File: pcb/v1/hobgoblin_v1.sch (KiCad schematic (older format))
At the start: 28 parts

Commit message: Finish the schematic
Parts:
- removed R?: 10K, symbol Device:R
- removed SW?: ROMBNK, symbol Switch:SW_DIP_x01
- removed U?: 74LS32, symbol 74xx:74LS32
- removed U?: 28C256, symbol Memory_EEPROM:28C256
- added C10, C11, C12, C2, C3, C4, C5, C6, C7, C8, C9: 0.1uF, Capacitor_THT:C_Disc_D3.8mm_W2.6mm_P2.50mm, symbol Device:C
- added CF1: CF_Socket, Connector_Card:CF-Card_3M_N7E50-7516PK-20-WF, symbol hobgoblin:CF_Socket
- added D2: CF, LED_THT:LED_D5.0mm, symbol Device:LED
- added D5: ON, LED_THT:LED_D5.0mm, symbol Device:LED
- added J1: 5V, Connector_BarrelJack:BarrelJack_Horizontal, symbol Connector:Barrel_Jack
- added J2: RC2014EXT1, Connector_PinHeader_2.54mm:PinHeader_1x40_P2.54mm_Vertical, symbol Connector_Generic:Conn_01x40
- added J3: RC2014EXT2, Connector_PinHeader_2.54mm:PinHeader_1x40_P2.54mm_Vertical, symbol Connector_Generic:Conn_01x40
- added R10, R14, R7, R8, R9: 1K, Resistor_THT:R_Axial_DIN0207_L6.3mm_D2.5mm_P10.16mm_Horizontal, symbol Device:R
- added R11: 330, Resistor_THT:R_Axial_DIN0207_L6.3mm_D2.5mm_P10.16mm_Horizontal, symbol Device:R
- added R4, R5, R6: 10K, Resistor_THT:R_Axial_DIN0207_L6.3mm_D2.5mm_P10.16mm_Horizontal, symbol Device:R
- added SW2: ROMBNK, Button_Switch_THT:SW_DIP_SPSTx03_Slide_6.7x9.18mm_W7.62mm_P2.54mm_LowProfile, symbol Switch:SW_DIP_x03
- added unit 3 of U7
- added unit 5 of U7
- added U8: SST39SF010, Package_DIP:DIP-32_W15.24mm_LongPads, symbol Memory_Flash:SST39SF010
- C1: renamed from C?; footprint (none) -> Capacitor_THT:C_Disc_D3.8mm_W2.6mm_P2.50mm
- R1, R2, R3: renamed from R?; footprint (none) -> Resistor_THT:R_Axial_DIN0207_L6.3mm_D2.5mm_P10.16mm_Horizontal
- SW1: renamed from SW?; footprint (none) -> Button_Switch_THT:SW_PUSH_6mm
- U1, U3, U6, U7: renamed from U?; footprint (none) -> Package_DIP:DIP-14_W7.62mm_LongPads
- U2: renamed from U?; footprint (none) -> Package_DIP:DIP-40_W15.24mm_LongPads
- U4: renamed from U?; footprint (none) -> Package_DIP:DIP-16_W7.62mm_LongPads
- U5: renamed from U?; footprint (none) -> Package_DIP:DIP-32_W15.24mm_LongPads
- U9: renamed from U?; footprint Package_DIP:DIP-40_W15.24mm -> Package_DIP:DIP-24_W15.24mm_LongPads
- gave numbers to parts that had none: 3
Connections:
- net labels added: IORQ, ROMBNK0, ROMBNK1, ROMBNK2, RXD, TXD, USR1, USR2, USR3, USR4, ~RTS
- net labels removed: ROMBNK, ~IORD, ~PORT0
- wire segments 53 -> 109
- no-connect marks 10 -> 27
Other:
- moved on the sheet: U1A, U1C, U1D, U4, U5, U6A, U6C, U6D, U7A, U7B, U9, X1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

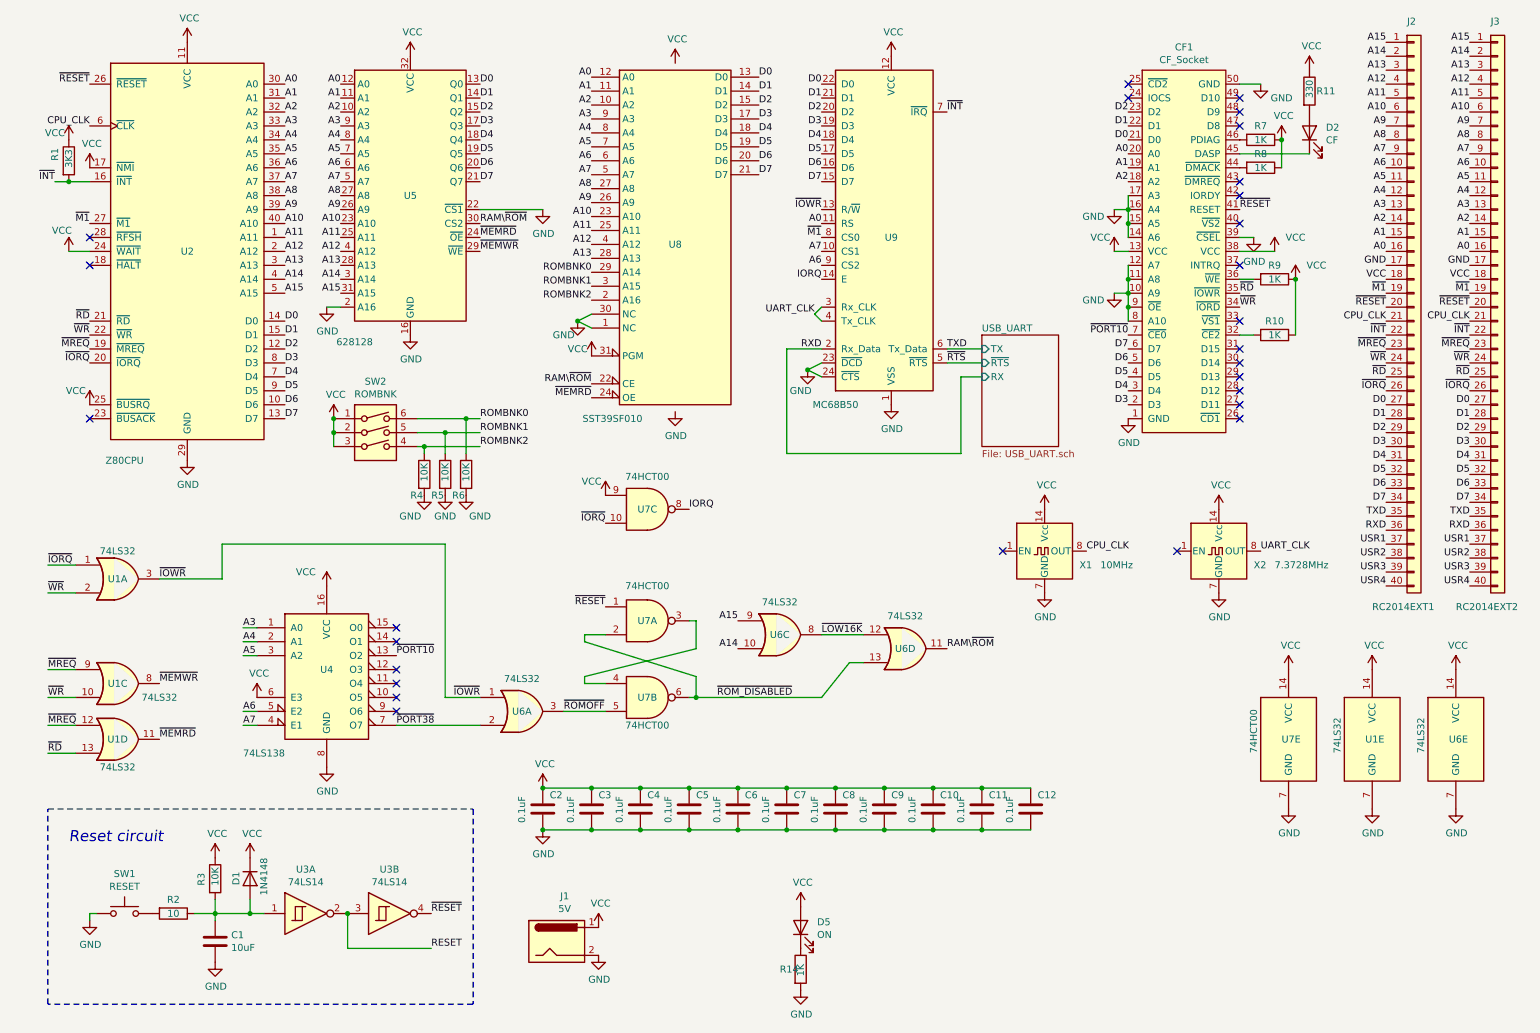
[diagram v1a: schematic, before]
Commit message: Place components on the PCB layout
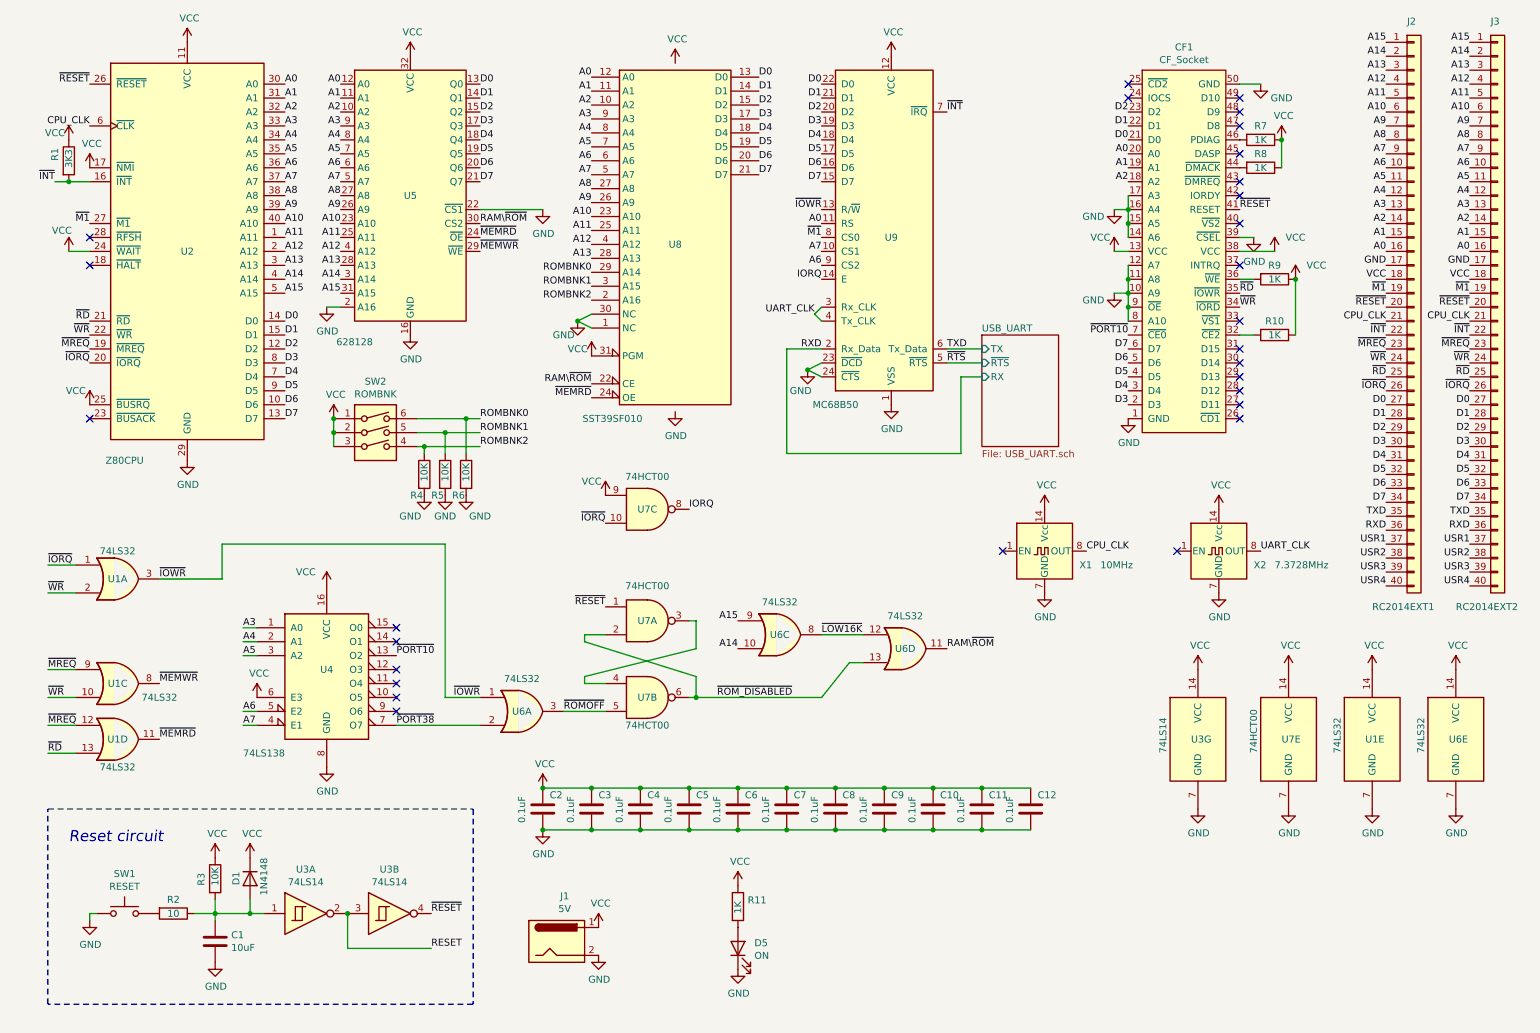
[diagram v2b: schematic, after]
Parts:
- removed D2: CF, LED_THT:LED_D5.0mm, symbol Device:LED
- removed R14: 1K, Resistor_THT:R_Axial_DIN0207_L6.3mm_D2.5mm_P10.16mm_Horizontal, symbol Device:R
- added unit 7 of U3
- J2, J3: footprint Connector_PinHeader_2.54mm:PinHeader_1x40_P2.54mm_Vertical -> hobgoblin:RC2014_Connector
- R11: value 330 -> 1K
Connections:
- net GND: now also D5.1 (K), U3.7 (GND)
- net VCC: now also U3.14 (VCC); no longer D5.2 (A)
- net at R11.2: now also D5.2 (A)
- no-connect marks 27 -> 28
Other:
- moved on the sheet: D5
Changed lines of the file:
@@
 F 0 "J3" H 10950 4650 50  0000 L CNN
 F 1 "RC2014EXT2" H 10700 450 50  0000 L CNN
-F 2 "Connector_PinHeader_2.54mm:PinHeader_1x40_P2.54mm_Vertical" H 11000 2600 50  0001 C CNN
+F 2 "hobgoblin:RC2014_Connector" H 11000 2600 50  0001 C CNN
 F 3 "~" H 11000 2600 50  0001 C CNN
 	1    11000 2600
@@
 F 0 "J2" H 10350 4650 50  0000 L CNN
 F 1 "RC2014EXT1" H 10100 450 50  0000 L CNN
-F 2 "Connector_PinHeader_2.54mm:PinHeader_1x40_P2.54mm_Vertical" H 10400 2600 50  0001 C CNN
+F 2 "hobgoblin:RC2014_Connector" H 10400 2600 50  0001 C CNN
 F 3 "~" H 10400 2600 50  0001 C CNN
 	1    10400 2600
@@
 Connection ~ 9450 1400
 $Comp
-L Device:LED D2
-U 1 1 5FF291EF
-P 9650 1350
-F 0 "D2" V 9689 1232 50  0000 R CNN
-F 1 "CF" V 9598 1232 50  0000 R CNN
-F 2 "LED_THT:LED_D5.0mm" H 9650 1350 50  0001 C CNN
-F 3 "~" H 9650 1350 50  0001 C CNN
-	1    9650 1350
-	0    -1   -1   0
-$EndComp
-Wire Wire Line
-	9650 1500 9150 1500
-$Comp
-L Device:R R11
-U 1 1 5FF2D25B
-P 9650 1050
-F 0 "R11" H 9700 1050 50  0000 L CNN
-F 1 "330" V 9650 1000 50  0000 L CNN
-F 2 "Resistor_THT:R_Axial_DIN0207_L6.3mm_D2.5mm_P10.16mm_Horizontal" V 9580 1050 50  0001 C CNN
-F 3 "~" H 9650 1050 50  0001 C CNN
-	1    9650 1050
-	1    0    0    -1
-$EndComp
-$Comp
-L power:VCC #PWR049
-U 1 1 5FF2F6DF
-P 9650 900
-F 0 "#PWR049" H 9650 750 50  0001 C CNN
-F 1 "VCC" H 9665 1073 50  0000 C CNN
-F 2 "" H 9650 900 50  0001 C CNN
-F 3 "" H 9650 900 50  0001 C CNN
-	1    9650 900
-	1    0    0    -1
-$EndComp
-$Comp
 L power:GND #PWR042
 U 1 1 5FF38D98
@@
 L Device:LED D5
 U 1 1 5FA5AC1B
-P 6000 7050
-F 0 "D5" V 6039 6932 50  0000 R CNN
-F 1 "ON" V 5948 6932 50  0000 R CNN
-F 2 "LED_THT:LED_D5.0mm" H 6000 7050 50  0001 C CNN
-F 3 "~" H 6000 7050 50  0001 C CNN
-	1    6000 7050
+P 5550 7200
+F 0 "D5" V 5589 7082 50  0000 R CNN
+F 1 "ON" V 5498 7082 50  0000 R CNN
+F 2 "LED_THT:LED_D5.0mm" H 5550 7200 50  0001 C CNN
+F 3 "~" H 5550 7200 50  0001 C CNN
+	1    5550 7200
 	0    -1   -1   0
 $EndComp
@@
 L power:GND #PWR0101
 U 1 1 5FA5C10E
-P 6000 7500
-F 0 "#PWR0101" H 6000 7250 50  0001 C CNN
-F 1 "GND" H 6005 7327 50  0000 C CNN
-F 2 "" H 6000 7500 50  0001 C CNN
-F 3 "" H 6000 7500 50  0001 C CNN
-	1    6000 7500
+P 5550 7350
+F 0 "#PWR0101" H 5550 7100 50  0001 C CNN
+F 1 "GND" H 5555 7177 50  0000 C CNN
+F 2 "" H 5550 7350 50  0001 C CNN
+F 3 "" H 5550 7350 50  0001 C CNN
+	1    5550 7350
+	1    0    0    -1
+$EndComp
+$Comp
+L 74xx:74LS14 U3
+U 7 1 6002B138
+P 8850 5700
+F 0 "U3" H 8800 5700 50  0000 L CNN
+F 1 "74LS14" V 8600 5600 50  0000 L CNN
+F 2 "Package_DIP:DIP-14_W7.62mm_LongPads" H 8850 5700 50  0001 C CNN
+F 3 "http://www.ti.com/lit/gpn/sn74LS14" H 8850 5700 50  0001 C CNN
+	7    8850 5700
+	1    0    0    -1
+$EndComp
+$Comp
+L power:VCC #PWR0104
+U 1 1 6002EF38
+P 8850 5200
+F 0 "#PWR0104" H 8850 5050 50  0001 C CNN
+F 1 "VCC" H 8865 5373 50  0000 C CNN
+F 2 "" H 8850 5200 50  0001 C CNN
+F 3 "" H 8850 5200 50  0001 C CNN
+	1    8850 5200
+	1    0    0    -1
+$EndComp
+$Comp
+L power:GND #PWR0105
+U 1 1 6002F3F6
+P 8850 6200
+F 0 "#PWR0105" H 8850 5950 50  0001 C CNN
+F 1 "GND" H 8855 6027 50  0000 C CNN
+F 2 "" H 8850 6200 50  0001 C CNN
+F 3 "" H 8850 6200 50  0001 C CNN
+	1    8850 6200
+	1    0    0    -1
+$EndComp
+NoConn ~ 9150 1500
+$Comp
+L Device:R R11
+U 1 1 60162B5D
+P 5550 6900
+F 0 "R11" H 5620 6946 50  0000 L CNN
+F 1 "1K" V 5550 6850 50  0000 L CNN
+F 2 "Resistor_THT:R_Axial_DIN0207_L6.3mm_D2.5mm_P10.16mm_Horizontal" V 5480 6900 50  0001 C CNN
+F 3 "~" H 5550 6900 50  0001 C CNN
+	1    5550 6900
 	1    0    0    -1
 $EndComp
 $Comp
 L power:VCC #PWR0102
-U 1 1 5FA5D7A5
-P 6000 6900
-F 0 "#PWR0102" H 6000 6750 50  0001 C CNN
-F 1 "VCC" H 6015 7073 50  0000 C CNN
-F 2 "" H 6000 6900 50  0001 C CNN
-F 3 "" H 6000 6900 50  0001 C CNN
-	1    6000 6900
-	1    0    0    -1
-$EndComp
-$Comp
-L Device:R R14
-U 1 1 5FA5F035
-P 6000 7350
-F 0 "R14" H 5850 7350 50  0000 L CNN
-F 1 "1K" V 6000 7300 50  0000 L CNN
-F 2 "Resistor_THT:R_Axial_DIN0207_L6.3mm_D2.5mm_P10.16mm_Horizontal" V 5930 7350 50  0001 C CNN
-F 3 "~" H 6000 7350 50  0001 C CNN
-	1    6000 7350
-	1    0    0    -1
-$EndComp
+U 1 1 601640F6
+P 5550 6750
+F 0 "#PWR0102" H 5550 6600 50  0001 C CNN
+F 1 "VCC" H 5565 6923 50  0000 C CNN
+F 2 "" H 5550 6750 50  0001 C CNN
+F 3 "" H 5550 6750 50  0001 C CNN
+	1    5550 6750
+	1    0    0    -1
+$EndComp

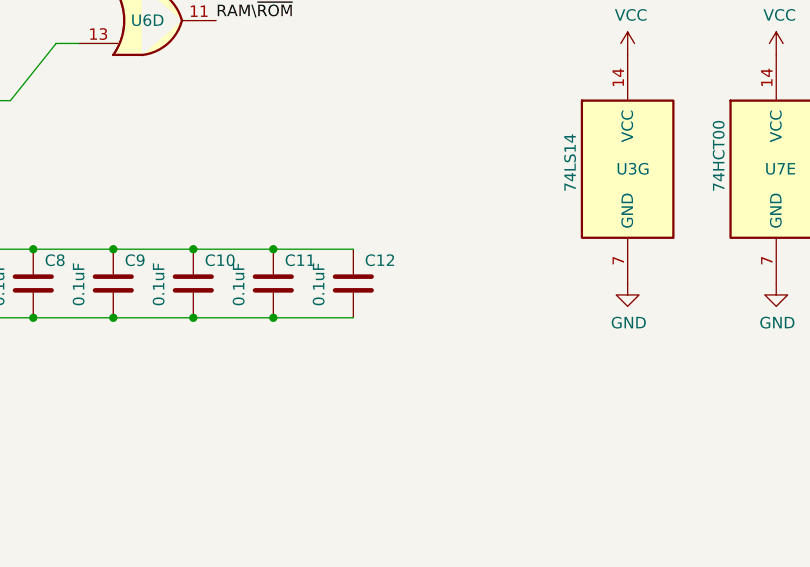
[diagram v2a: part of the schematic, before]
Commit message: Finish PCB layout
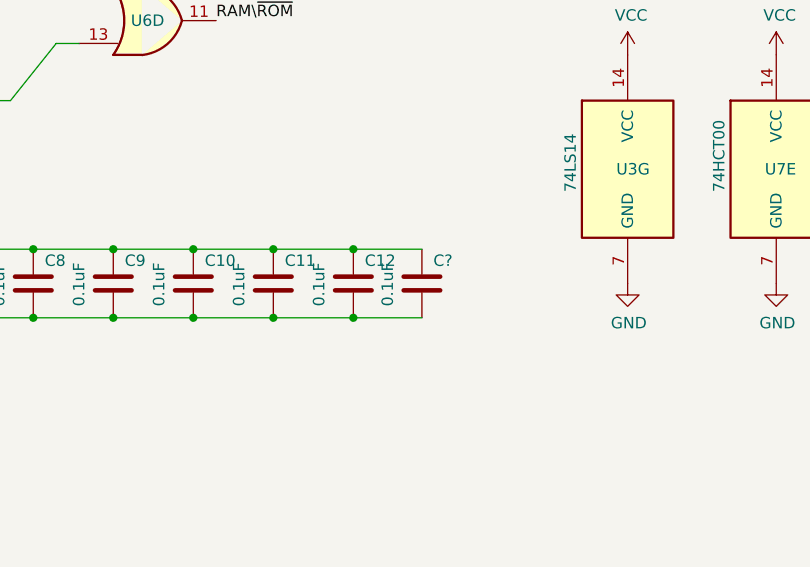
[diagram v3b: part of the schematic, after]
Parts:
- added C?: 0.1uF, Capacitor_THT:C_Disc_D3.8mm_W2.6mm_P2.50mm, symbol Device:C
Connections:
- net GND: now also C?.2
- net VCC: now also C?.1
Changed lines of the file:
@@
 	1    0    0    -1
 $EndComp
+$Comp
+L Device:C C?
+U 1 1 60AE0FC1
+P 7950 6200
+F 0 "C?" H 8000 6300 50  0000 L CNN
+F 1 "0.1uF" V 7800 6100 50  0000 L CNN
+F 2 "Capacitor_THT:C_Disc_D3.8mm_W2.6mm_P2.50mm" H 7988 6050 50  0001 C CNN
+F 3 "~" H 7950 6200 50  0001 C CNN
+	1    7950 6200
+	1    0    0    -1
+$EndComp
+Wire Wire Line
+	7650 6050 7950 6050
+Connection ~ 7650 6050
+Wire Wire Line
+	7650 6350 7950 6350
+Connection ~ 7650 6350
 $EndSCHEMATC

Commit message: Add UART socket and other PCB improvements
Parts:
- removed X1: 10MHz, Oscillator:Oscillator_DIP-14, symbol Oscillator:CXO_DIP14
- removed X2: 7.3728MHz, Oscillator:Oscillator_DIP-14, symbol Oscillator:CXO_DIP14
- added X1: 10MHz, Oscillator:Oscillator_DIP-8, symbol Oscillator:CXO_DIP8
- added X2: 7.3728MHz, Oscillator:Oscillator_DIP-8, symbol Oscillator:CXO_DIP8
- gave numbers to parts that had none: 1
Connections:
- net CPU_CLK: now also X1.5 (OUT)
- net GND: now also X1.4 (GND), X2.4 (GND)
- net UART_CLK: now also X2.5 (OUT)
- net VCC: now also X1.8 (Vcc), X2.8 (Vcc)
- net ~IOWR: no longer U9.13 (R/~W)
- net ~RD: now also CF1.34 (~IORD); no longer CF1.35 (~IOWR)
- net ~WR: now also CF1.35 (~IOWR), U9.13 (R/~W); no longer CF1.34 (~IORD)
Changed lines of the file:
@@
 ~RESET
-$Comp
-L Oscillator:CXO_DIP14 X1
-U 1 1 5F8D5383
-P 7750 4350
-F 0 "X1" H 8000 4250 50  0000 L CNN
-F 1 "10MHz" H 8150 4250 50  0000 L CNN
-F 2 "Oscillator:Oscillator_DIP-14" H 8200 4000 50  0001 C CNN
-F 3 "http://cdn-reichelt.de/documents/datenblatt/B400/OSZI.pdf" H 7650 4350 50  0001 C CNN
-	1    7750 4350
-	1    0    0    -1
-$EndComp
 $Comp
 L power:GND #PWR035
@@
 Text Label 8050 4350 0    50   ~ 0
 CPU_CLK
-$Comp
-L Oscillator:CXO_DIP14 X2
-U 1 1 5F8D7F95
-P 9000 4350
-F 0 "X2" H 9250 4250 50  0000 L CNN
-F 1 "7.3728MHz" H 9400 4250 50  0000 L CNN
-F 2 "Oscillator:Oscillator_DIP-14" H 9450 4000 50  0001 C CNN
-F 3 "http://cdn-reichelt.de/documents/datenblatt/B400/OSZI.pdf" H 8900 4350 50  0001 C CNN
-	1    9000 4350
-	1    0    0    -1
-$EndComp
 $Comp
 L power:GND #PWR041
@@
 NoConn ~ 9150 1800
 NoConn ~ 9150 1700
+Text Label 9150 2600 0    50   ~ 0
+~RD
 Text Label 9150 2500 0    50   ~ 0
-~RD
-Text Label 9150 2600 0    50   ~ 0
 ~WR
 NoConn ~ 9150 2300
@@
 Text Label 6150 2400 2    50   ~ 0
 IORQ
-Text Label 6150 1900 2    50   ~ 0
-~IOWR
 Wire Wire Line
 	600  5800 800  5800
@@
 $EndComp
 $Comp
-L Device:C C?
+L Device:C C16
 U 1 1 60AE0FC1
 P 7950 6200
-F 0 "C?" H 8000 6300 50  0000 L CNN
+F 0 "C16" H 8000 6300 50  0000 L CNN
 F 1 "0.1uF" V 7800 6100 50  0000 L CNN
 F 2 "Capacitor_THT:C_Disc_D3.8mm_W2.6mm_P2.50mm" H 7988 6050 50  0001 C CNN
@@
 	7650 6350 7950 6350
 Connection ~ 7650 6350
+$Comp
+L Oscillator:CXO_DIP8 X2
+U 1 1 60B385BD
+P 9000 4350
+F 0 "X2" H 8800 4100 50  0000 L CNN
+F 1 "7.3728MHz" H 9100 4100 50  0000 L CNN
+F 2 "Oscillator:Oscillator_DIP-8" H 9450 4000 50  0001 C CNN
+F 3 "http://cdn-reichelt.de/documents/datenblatt/B400/OSZI.pdf" H 8900 4350 50  0001 C CNN
+	1    9000 4350
+	1    0    0    -1
+$EndComp
+$Comp
+L Oscillator:CXO_DIP8 X1
+U 1 1 60B39F6D
+P 7750 4350
+F 0 "X1" H 7550 4100 50  0000 L CNN
+F 1 "10MHz" H 7850 4100 50  0000 L CNN
+F 2 "Oscillator:Oscillator_DIP-8" H 8200 4000 50  0001 C CNN
+F 3 "http://cdn-reichelt.de/documents/datenblatt/B400/OSZI.pdf" H 7650 4350 50  0001 C CNN
+	1    7750 4350
+	1    0    0    -1
+$EndComp
+Text Label 6150 1900 2    50   ~ 0
+~WR
 $EndSCHEMATC

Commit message: PCB: final touches
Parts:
- added D2: CF_BUSY, LED_THT:LED_D3.0mm, symbol Device:LED
- added R15: 1K, Resistor_THT:R_Axial_DIN0207_L6.3mm_D2.5mm_P10.16mm_Horizontal, symbol Device:R
- D5: footprint LED_THT:LED_D5.0mm -> LED_THT:LED_D3.0mm
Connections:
- net VCC: now also R15.1
- net at CF1.45 (DASP): now also D2.1 (K)
- new net: D2.2 (A), R15.2
- no-connect marks 28 -> 27
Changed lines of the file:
@@
 F 0 "D5" V 5589 7082 50  0000 R CNN
 F 1 "ON" V 5498 7082 50  0000 R CNN
-F 2 "LED_THT:LED_D5.0mm" H 5550 7200 50  0001 C CNN
+F 2 "LED_THT:LED_D3.0mm" H 5550 7200 50  0001 C CNN
 F 3 "~" H 5550 7200 50  0001 C CNN
 	1    5550 7200
@@
 	1    0    0    -1
 $EndComp
-NoConn ~ 9150 1500
 $Comp
 L Device:R R11
@@
 Text Label 6150 1900 2    50   ~ 0
 ~WR
+$Comp
+L Device:LED D2
+U 1 1 60C66287
+P 9750 1350
+F 0 "D2" V 9789 1232 50  0000 R CNN
+F 1 "CF_BUSY" H 9900 1450 50  0000 R CNN
+F 2 "LED_THT:LED_D3.0mm" H 9750 1350 50  0001 C CNN
+F 3 "~" H 9750 1350 50  0001 C CNN
+	1    9750 1350
+	0    -1   -1   0
+$EndComp
+Wire Wire Line
+	9150 1500 9750 1500
+$Comp
+L Device:R R15
+U 1 1 60C6B74B
+P 9750 1050
+F 0 "R15" H 9820 1096 50  0000 L CNN
+F 1 "1K" V 9750 1000 50  0000 L CNN
+F 2 "Resistor_THT:R_Axial_DIN0207_L6.3mm_D2.5mm_P10.16mm_Horizontal" V 9680 1050 50  0001 C CNN
+F 3 "~" H 9750 1050 50  0001 C CNN
+	1    9750 1050
+	1    0    0    -1
+$EndComp
+$Comp
+L power:VCC #PWR069
+U 1 1 60C6CC9F
+P 9750 900
+F 0 "#PWR069" H 9750 750 50  0001 C CNN
+F 1 "VCC" H 9765 1073 50  0000 C CNN
+F 2 "" H 9750 900 50  0001 C CNN
+F 3 "" H 9750 900 50  0001 C CNN
+	1    9750 900
+	1    0    0    -1
+$EndComp
 $EndSCHEMATC

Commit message: Fix the CF card slot footprint (v1.1.)
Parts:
- CF1: footprint Connector_Card:CF-Card_3M_N7E50-7516PK-20-WF -> hobgoblin:CF-Card_3M_N7E50-7516PK-20-WF
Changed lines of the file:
@@
 F 0 "CF1" H 8750 3765 50  0000 C CNN
 F 1 "CF_Socket" H 8750 3674 50  0000 C CNN
-F 2 "Connector_Card:CF-Card_3M_N7E50-7516PK-20-WF" H 8750 2250 50  0001 C CNN
+F 2 "hobgoblin:CF-Card_3M_N7E50-7516PK-20-WF" H 8750 2250 50  0001 C CNN
 F 3 "" H 8750 2250 50  0001 C CNN
 	1    8750 2250

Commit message: Fix CF footprint pin numbering
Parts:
- C1: footprint Capacitor_THT:C_Disc_D3.8mm_W2.6mm_P2.50mm -> Capacitor_THT:CP_Radial_D4.0mm_P1.50mm
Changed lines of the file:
@@
 F 0 "C1" H 1915 7196 50  0000 L CNN
 F 1 "10uF" H 1915 7105 50  0000 L CNN
-F 2 "Capacitor_THT:C_Disc_D3.8mm_W2.6mm_P2.50mm" H 1838 7000 50  0001 C CNN
+F 2 "Capacitor_THT:CP_Radial_D4.0mm_P1.50mm" H 1838 7000 50  0001 C CNN
 F 3 "~" H 1800 7150 50  0001 C CNN
 	1    1800 7150
